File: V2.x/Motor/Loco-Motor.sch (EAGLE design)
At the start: 48 parts, among them IC1 Atmega 328-P, IC2 MCP2515, IC3 LM340MP-05, Q1 8MHz, Q2 16MHz

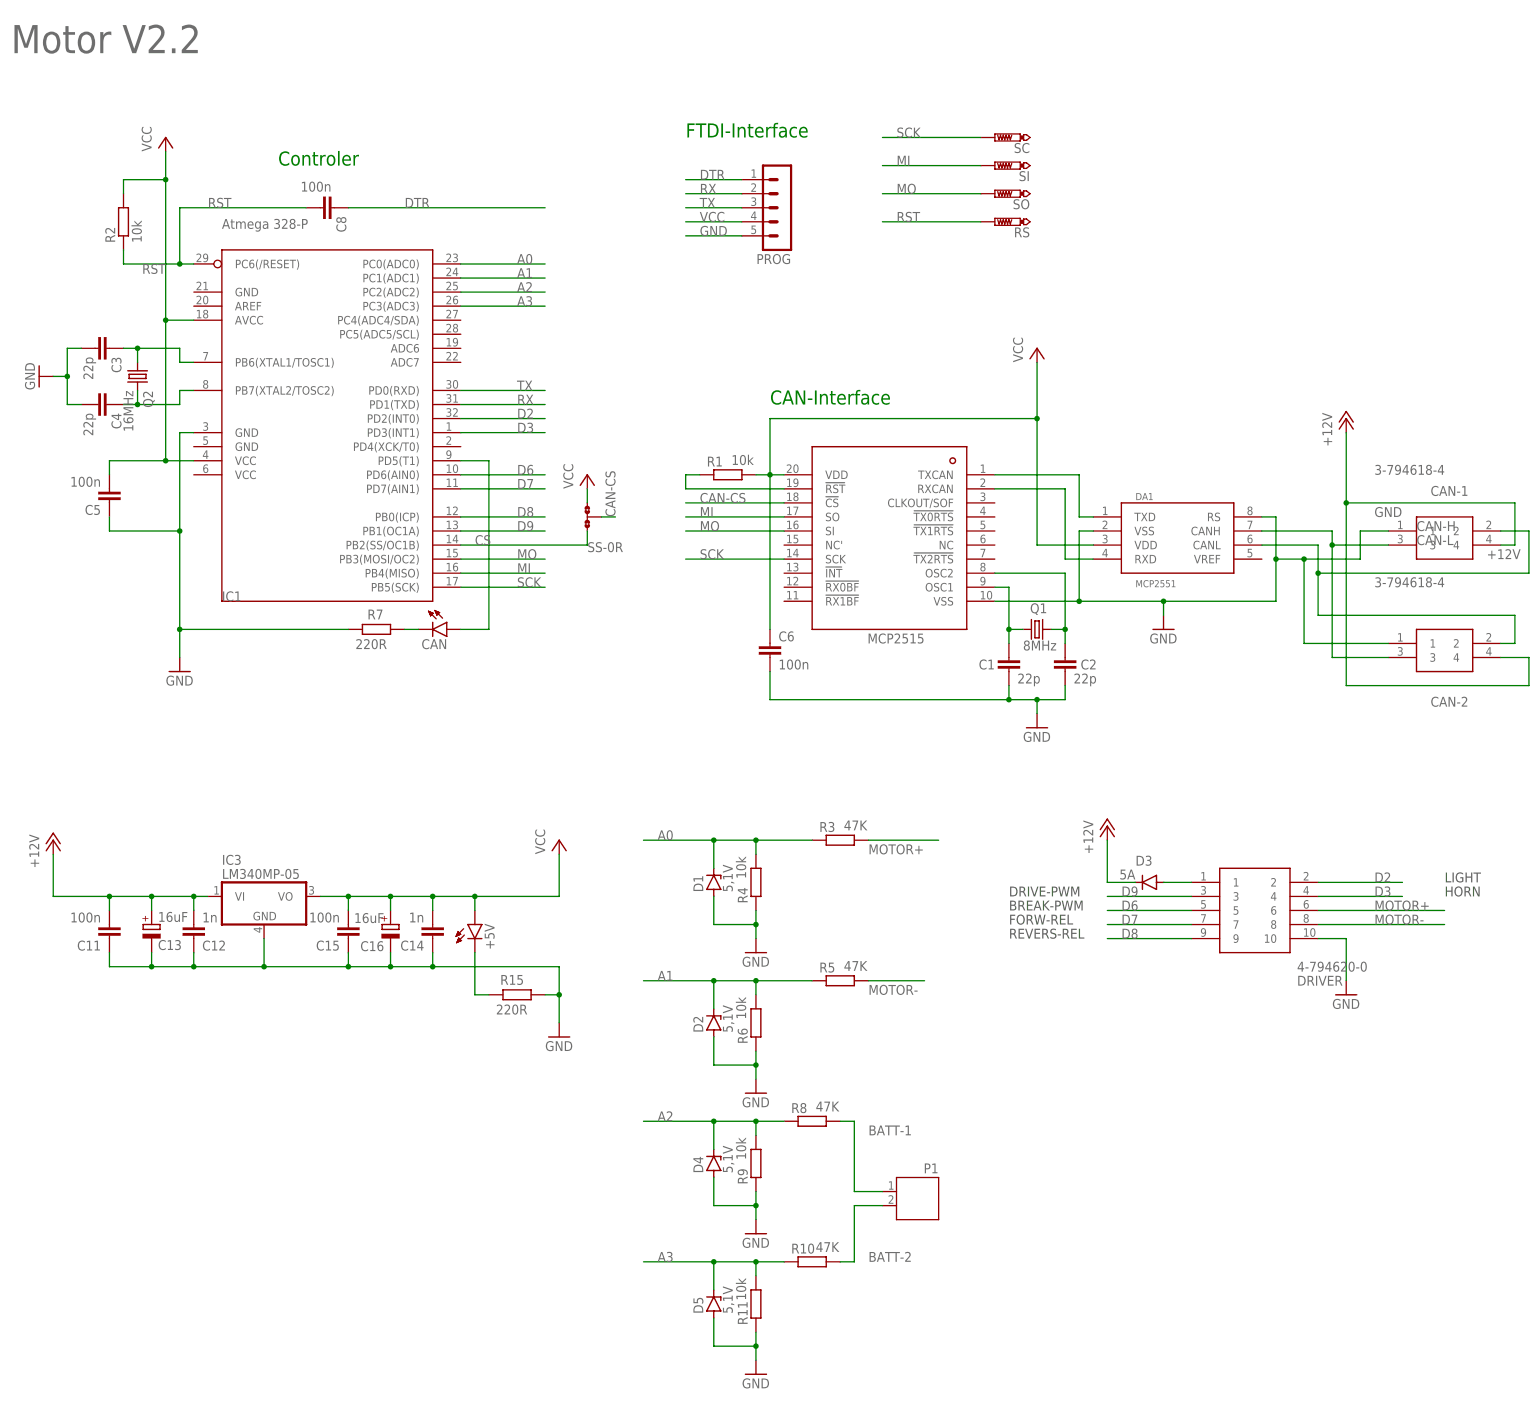
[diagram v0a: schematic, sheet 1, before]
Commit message: changed sch and brd of motor and switch for RX/TX leds
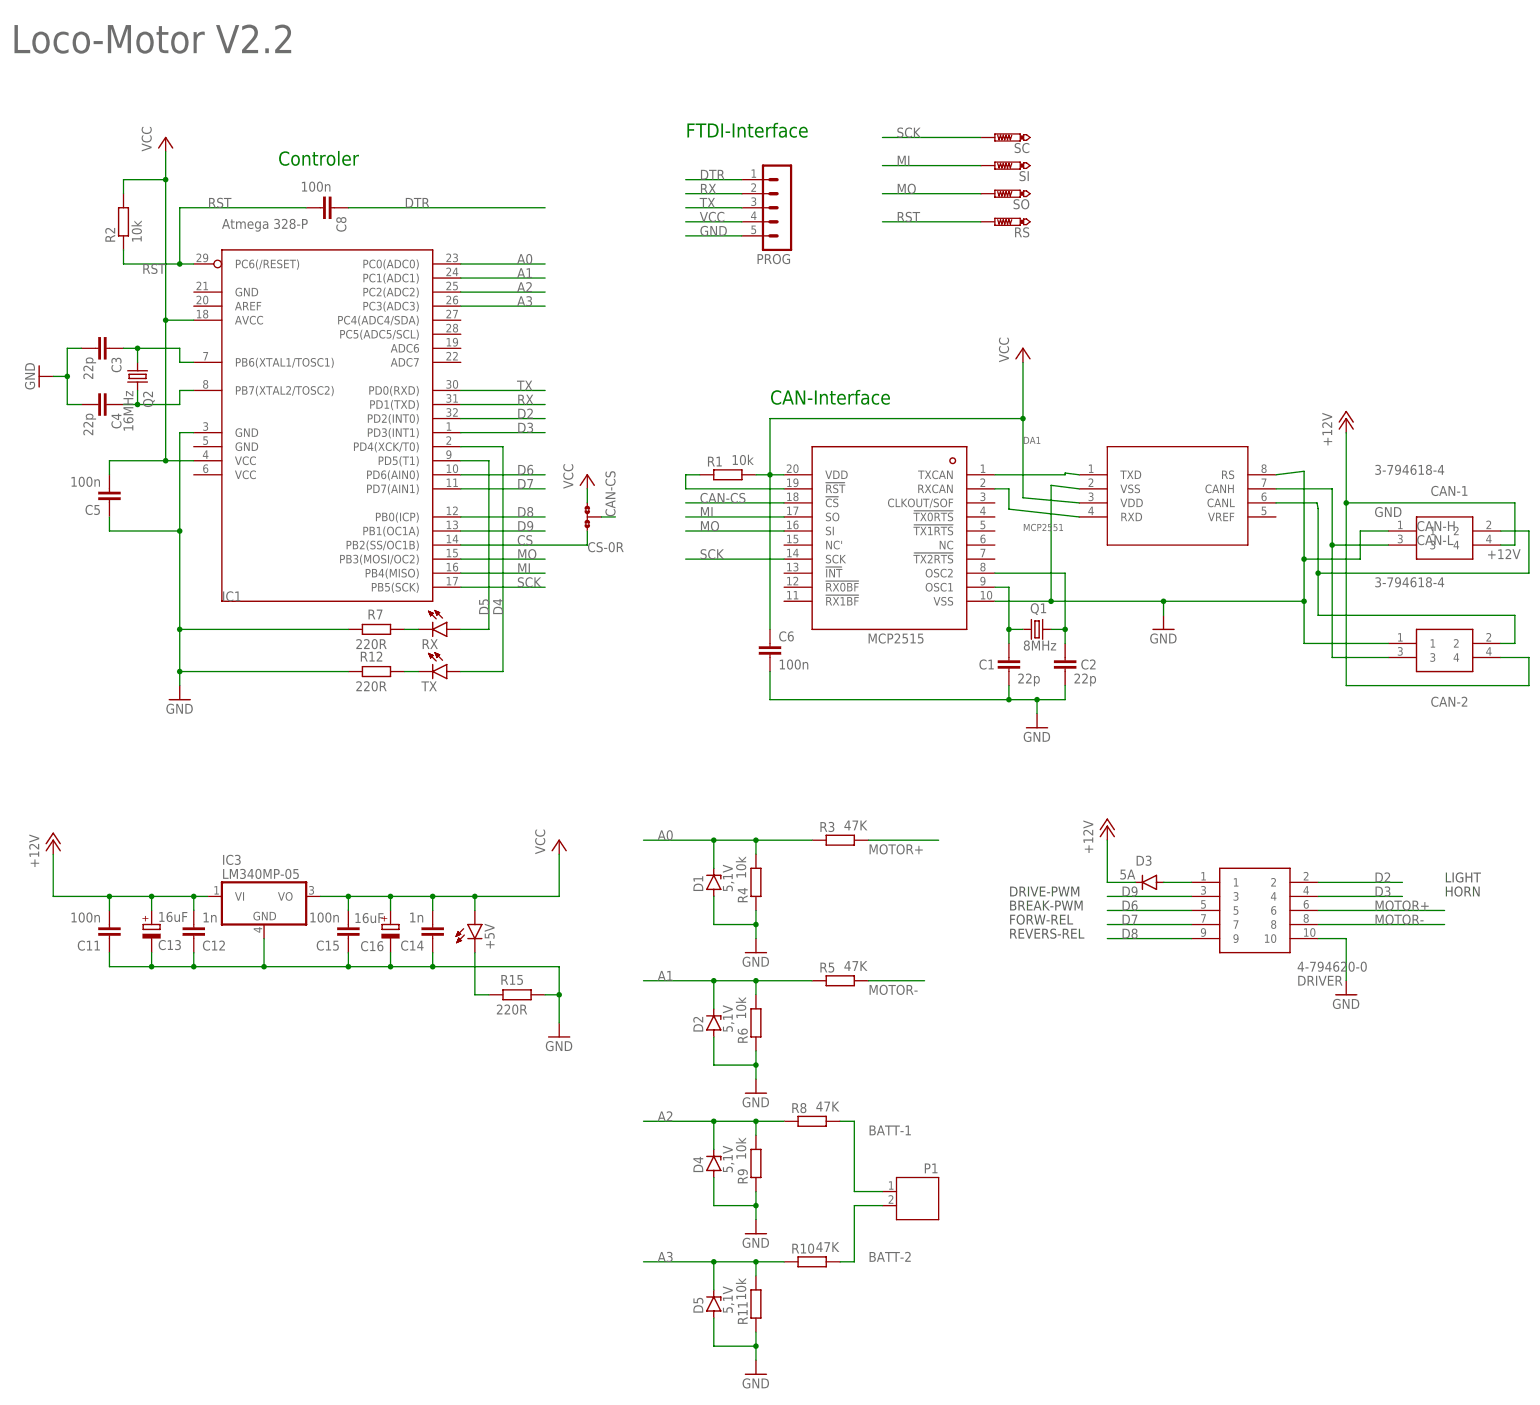
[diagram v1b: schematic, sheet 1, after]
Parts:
- added R12: 220R, rcl:R-EU_R0805
- added TX: (no value), led:LEDCHIP-LED0603
- CAN-1, CAN-2: device SamacSys_Parts:3-794618-4 -> Micro Mate-N-Lok:3-794618-4
- DA1: device TJA1050:TJA1050 -> MCP2551:MCP2551-X/SNSOIC8-N_MC_MCH
- IC1: device atmel:MEGA8-AI -> atmel:MEGA8
- IC2: device mcp2514:MCP2515 -> MCP2515:MCP2515
- PROG: device con-lstb:MA05-1 -> lst-b:MA05-1
- renumbered CAN to RX, SS to CS
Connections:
- net N$3 renamed D5
- new net D4: IC1.PD4(XCK/T0), TX.A
- new net N$4: R12.1, TX.C
- net GND: now also R12.2
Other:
- note added: "Loco-Motor V2.2"
- note removed: "Motor V2.2"
